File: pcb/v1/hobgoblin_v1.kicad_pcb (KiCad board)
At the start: 2 copper layers, 54 parts, among them J1 5V, J2 RC2014EXT1, J3 RC2014EXT2, J4 USB_B_Mini, SW1 RESET, SW2 ROMBNK, U1 74LS32, U10 FT232RL, U2 Z80CPU, U3 74LS14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

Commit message: Place components on the PCB layout
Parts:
- J2, J3: footprint Connector_PinHeader_2.54mm:PinHeader_1x40_P2.54mm_Vertical -> hobgoblin:RC2014_Connector
- R11: value 330 -> 1K
- moved C12 183.3 mm to (57.0, 106.5), turned to 180 degrees
- moved C11 164.8 mm to (31.0, 68.2), turned to 90 degrees
- moved C9 146.9 mm to (55.0, 68.5), turned to 90 degrees
- moved C1 144.6 mm to (97.5, 110.0), turned to 90 degrees
- moved C3 142.4 mm to (45.7, 68.5), turned to 90 degrees
- moved R6 140.5 mm to (113.5, 30.5), turned to 180 degrees
- moved R2 135.3 mm to (94.5, 89.5), turned to 270 degrees
- moved R8 132.6 mm to (114.0, 89.5), turned to 270 degrees
- moved C6 132.5 mm to (73.5, 107.0), turned to 180 degrees
- moved J2 131.1 mm to (28.0, 25.0), turned to 0 degrees
- moved JP1 118.9 mm to (159.5, 31.0), turned to 180 degrees
- moved J3 116.4 mm to (42.7, 25.0), turned to 0 degrees
- moved D1 113.6 mm to (89.5, 98.5), turned to 90 degrees
- moved C7 107.0 mm to (105.5, 107.0), turned to 180 degrees
- moved C10 106.7 mm to (121.5, 105.0), turned to 180 degrees
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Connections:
- D5 pad 1: Net-(D5-Pad1) -> GND
- D5 pad 2: VCC -> Net-(D5-Pad2)
- R11 pad 2: Net-(D2-Pad2) -> Net-(D5-Pad2)
- U3 pad 14: (no net) -> VCC
- U3 pad 7: (no net) -> GND
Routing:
- added copper zone on B.Cu, net GND
- added copper zone on F.Cu, net GND
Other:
- board outline added: 160 x 110 mm
- board text added: "Pin1"

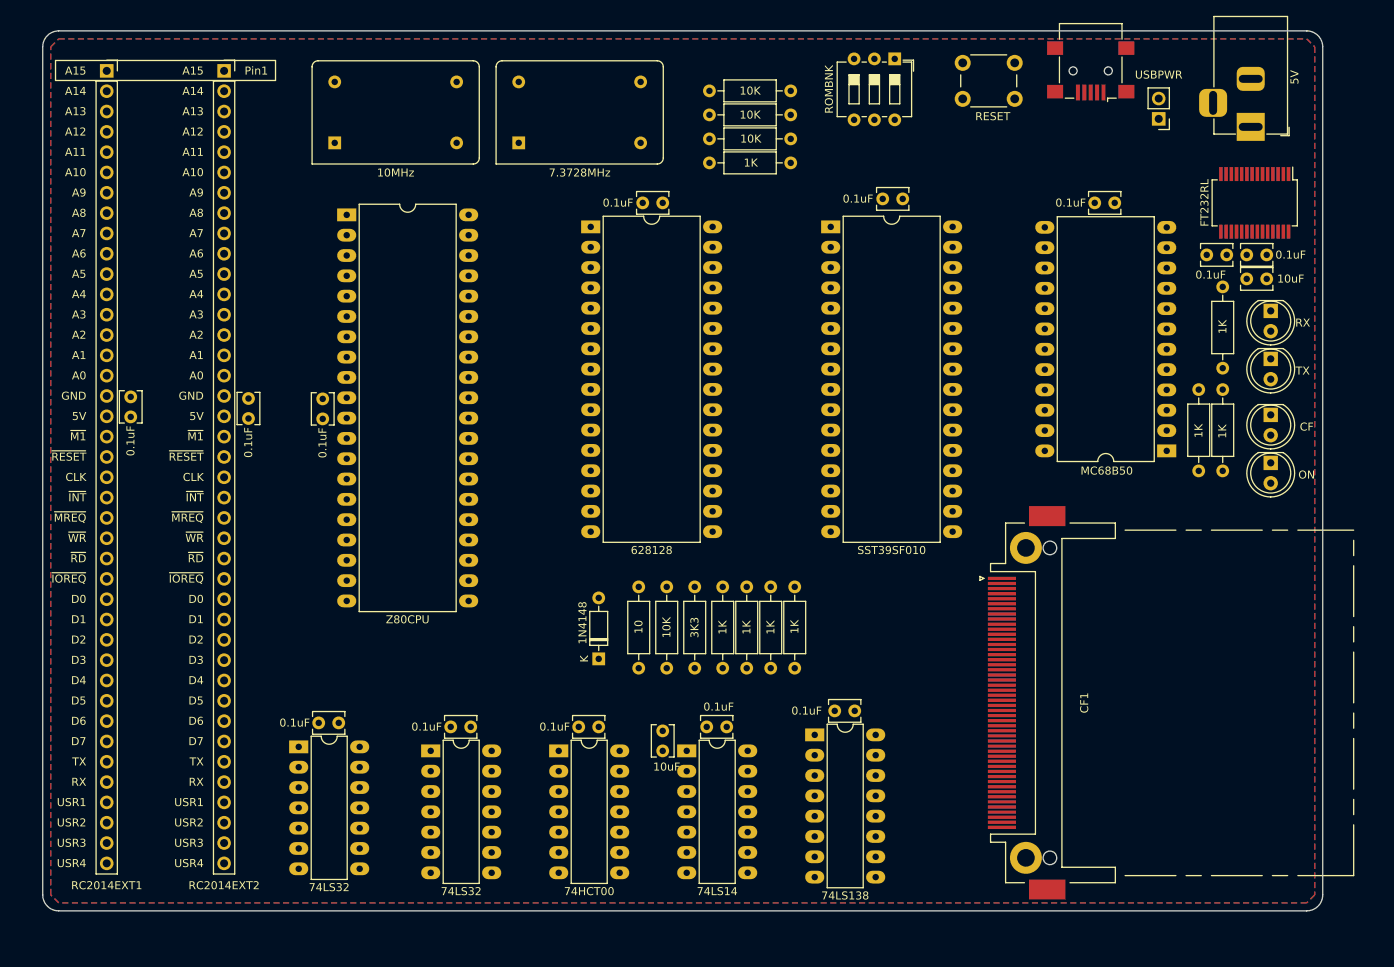
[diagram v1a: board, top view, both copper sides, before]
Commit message: Finish PCB layout
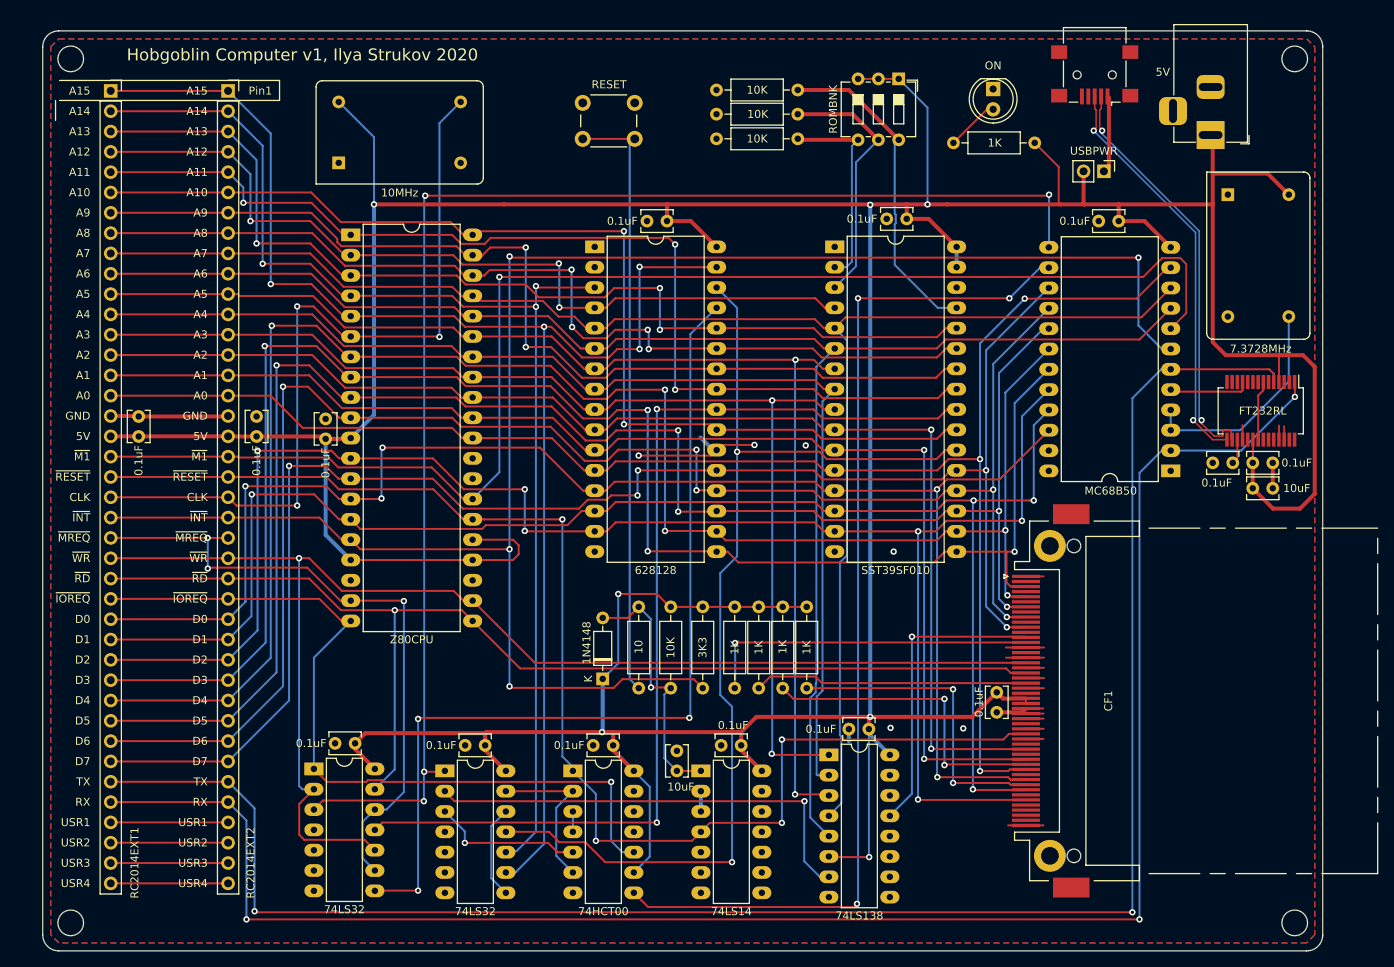
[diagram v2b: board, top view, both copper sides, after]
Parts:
- removed D2: CF, LED_THT:LED_D5.0mm
- removed D3: TX, LED_THT:LED_D5.0mm
- removed D4: RX, LED_THT:LED_D5.0mm
- removed R12, R13, R14: 1K, Resistor_THT:R_Axial_DIN0207_L6.3mm_D2.5mm_P10.16mm_Horizontal
- added C16: 0.1uF, Capacitor_THT:C_Disc_D3.8mm_W2.6mm_P2.50mm, F.Cu at (139.3, 102.7)
- added REF**: M3, MountingHole:MountingHole_3.2mm_M3, F.Cu at (176.5, 131.5)
- added REF**: M3, MountingHole:MountingHole_3.2mm_M3, F.Cu at (23.5, 131.5)
- added REF**: M3, MountingHole:MountingHole_3.2mm_M3, F.Cu at (23.5, 23.5)
- added REF**: M3, MountingHole:MountingHole_3.2mm_M3, F.Cu at (176.5, 23.5)
- moved X2 88.9 mm to (168.1, 40.5), turned to 270 degrees
- moved D5 58.2 mm to (138.8, 27.3)
- moved SW1 47.8 mm to (87.5, 29.0)
- moved R11 45.8 mm to (144.0, 34.0), turned to 180 degrees
- moved C13 26.2 mm to (171.3, 77.2)
- moved C14 26.0 mm to (171.3, 74.0)
- moved C15 26.0 mm to (166.3, 74.0)
- moved U10 26.0 mm to (172.3, 67.5)
- moved JP1 9.48 mm to (152.6, 37.6), turned to 270 degrees
- moved R7 7.91 mm to (115.5, 92.0)
- moved R4 6.05 mm to (114.4, 33.5)
- moved R10 5.15 mm to (106.5, 92.0)
- moved R9 5.15 mm to (109.5, 92.0)
- moved J1 5.11 mm to (166.0, 33.0)
- moved U1 3.34 mm to (53.9, 112.3)
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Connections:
- net Net-(J4-Pad2) renamed /USB_UART/USBD-
- net Net-(J4-Pad3) renamed /USB_UART/USBD+
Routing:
- net VCC: track 0.00 -> 635.4 mm, vias 0 -> 7
- net /TXD: track 0.00 -> 226.7 mm, vias 0 -> 2
- net /RXD: track 0.00 -> 223.0 mm, vias 0 -> 3
- net /~INT: track 0.00 -> 222.8 mm, vias 0 -> 4
- net /D4: track 0.00 -> 213.9 mm, vias 0 -> 5
- net /D2: track 0.00 -> 211.5 mm, vias 0 -> 6
- net /D5: track 0.00 -> 208.0 mm, vias 0 -> 5
- net /D3: track 0.00 -> 206.2 mm, vias 0 -> 4
- net /D6: track 0.00 -> 205.7 mm, vias 0 -> 5
- net /A6: track 0.00 -> 202.6 mm
- net /A7: track 0.00 -> 202.1 mm
- net /A0: track 0.00 -> 201.1 mm, vias 0 -> 3
- net /D7: track 0.00 -> 198.0 mm, vias 0 -> 5
- net /D0: track 0.00 -> 193.8 mm, vias 0 -> 5
- net /D1: track 0.00 -> 190.9 mm, vias 0 -> 4
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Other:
- board size 160 x 110 mm -> 160 x 115 mm
- board text added: "Hobgoblin Computer v1, Ilya Strukov 2020"

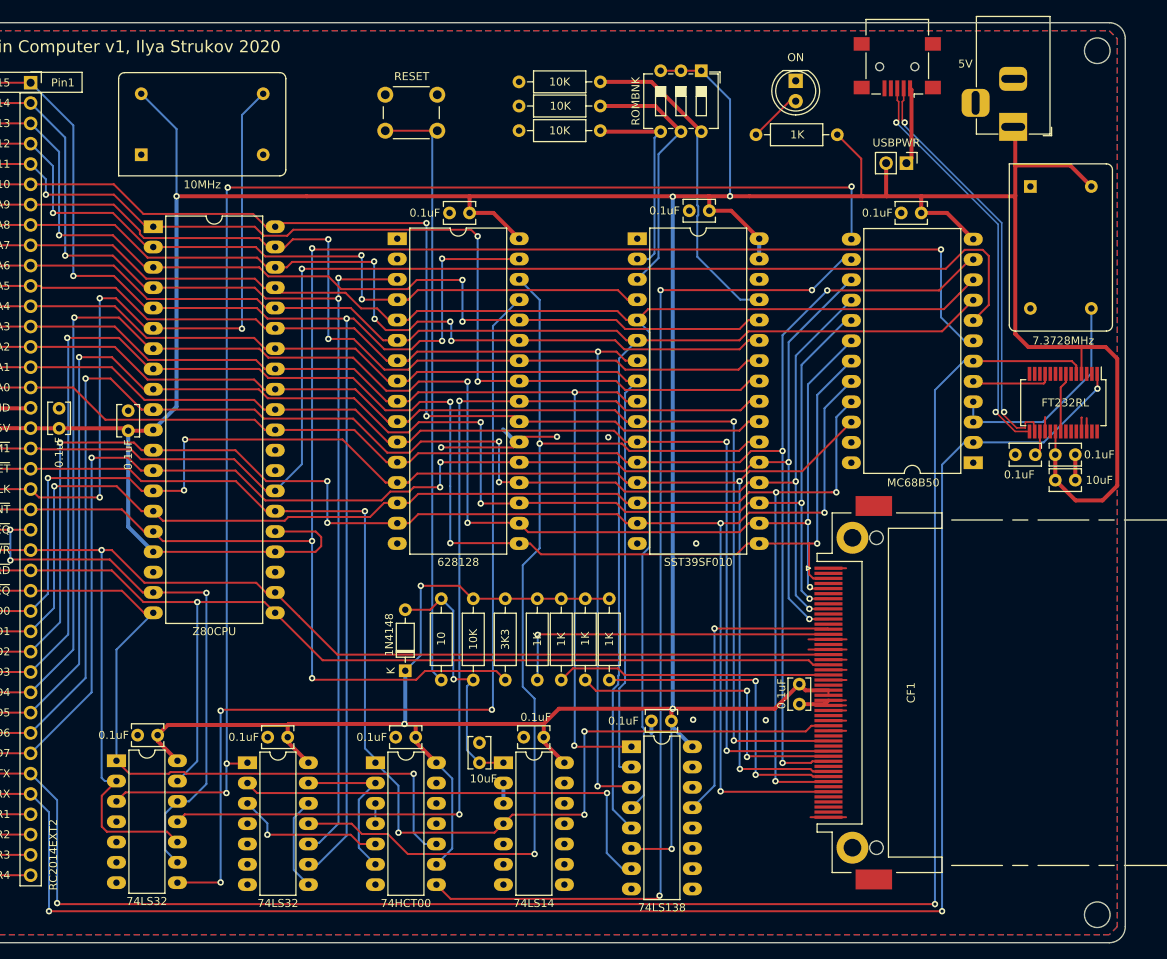
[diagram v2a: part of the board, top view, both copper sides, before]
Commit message: Add UART socket and other PCB improvements
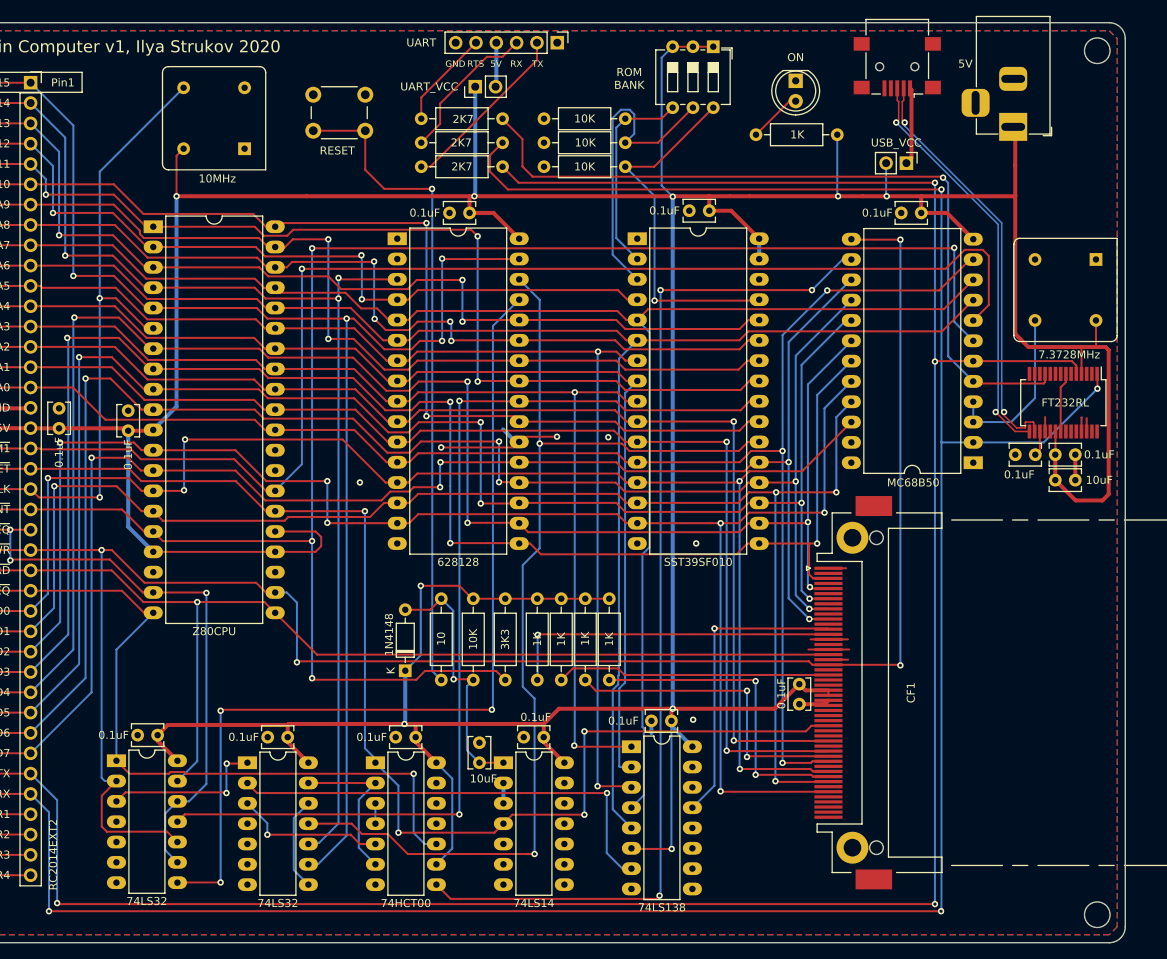
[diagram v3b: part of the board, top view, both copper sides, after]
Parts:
- added J5: UART, Connector_PinHeader_2.54mm:PinHeader_1x06_P2.54mm_Vertical, F.Cu at (109.0, 22.5)
- added JP2: UART_VCC, Connector_PinHeader_2.54mm:PinHeader_1x02_P2.54mm_Vertical, F.Cu at (98.8, 28.0)
- added R12: 2K7, Resistor_THT:R_Axial_DIN0207_L6.3mm_D2.5mm_P10.16mm_Horizontal, F.Cu at (92.0, 38.0)
- added R13: 2K7, Resistor_THT:R_Axial_DIN0207_L6.3mm_D2.5mm_P10.16mm_Horizontal, F.Cu at (92.0, 35.0)
- added R14: 2K7, Resistor_THT:R_Axial_DIN0207_L6.3mm_D2.5mm_P10.16mm_Horizontal, F.Cu at (92.0, 32.0)
- JP1: value USBPWR -> USB_VCC
- X1, X2: footprint Oscillator:Oscillator_DIP-14 -> Oscillator:Oscillator_DIP-8
- moved X1 12.9 mm to (69.9, 35.8), turned to 90 degrees
- moved X2 12.3 mm to (176.3, 49.6), turned to 180 degrees
- moved R6 11.1 mm to (117.5, 38.0)
- moved SW1 9.00 mm to (78.5, 29.0)
- moved R5 5.55 mm to (117.5, 35.0)
- moved R4 3.46 mm to (117.5, 32.0)
- moved SW2 3.35 mm to (128.5, 23.0)
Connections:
- CF1 pad 34: /~WR -> /~RD
- CF1 pad 35: /~RD -> /~WR
- U9 pad 13: /~IOWR -> /~WR
- X1 pad 8: /CPU_CLK -> VCC
- X2 pad 8: /UART_CLK -> VCC
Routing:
- net /~IOWR: track 177.3 -> 20.6 mm, vias 4 -> 2
- net /RXD: track 223.0 -> 317.8 mm, vias 3 -> 4
- net /~RTS: track 10.2 -> 97.4 mm, vias 0 -> 1
- net /TXD: track 226.7 -> 306.1 mm, vias 2 -> 4
- net /~WR: track 167.0 -> 240.4 mm, vias 1 -> 4
- net Net-(J5-Pad2): track 0.00 -> 22.2 mm
- net GND: track 88.3 -> 69.0 mm
- net Net-(J5-Pad3): track 0.00 -> 18.6 mm
- net Net-(J5-Pad5): track 0.00 -> 12.3 mm
- net /CPU_CLK: track 98.5 -> 87.5 mm, vias 3 -> 2
- net /ROMBNK1: track 32.1 -> 39.1 mm
- net /UART_CLK: track 27.9 -> 21.2 mm
- net Net-(R2-Pad2): track 75.9 -> 82.6 mm, vias 0 -> 1
- net Net-(J5-Pad4): track 0.00 -> 5.54 mm
- net /ROMBNK0: track 41.1 -> 45.4 mm, vias 0 -> 1
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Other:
- board text added: "5V"
- board text added: "GND"
- board text added: "ROM BANK"
- board text added: "RTS"
- board text added: "RX"
- board text added: "TX"

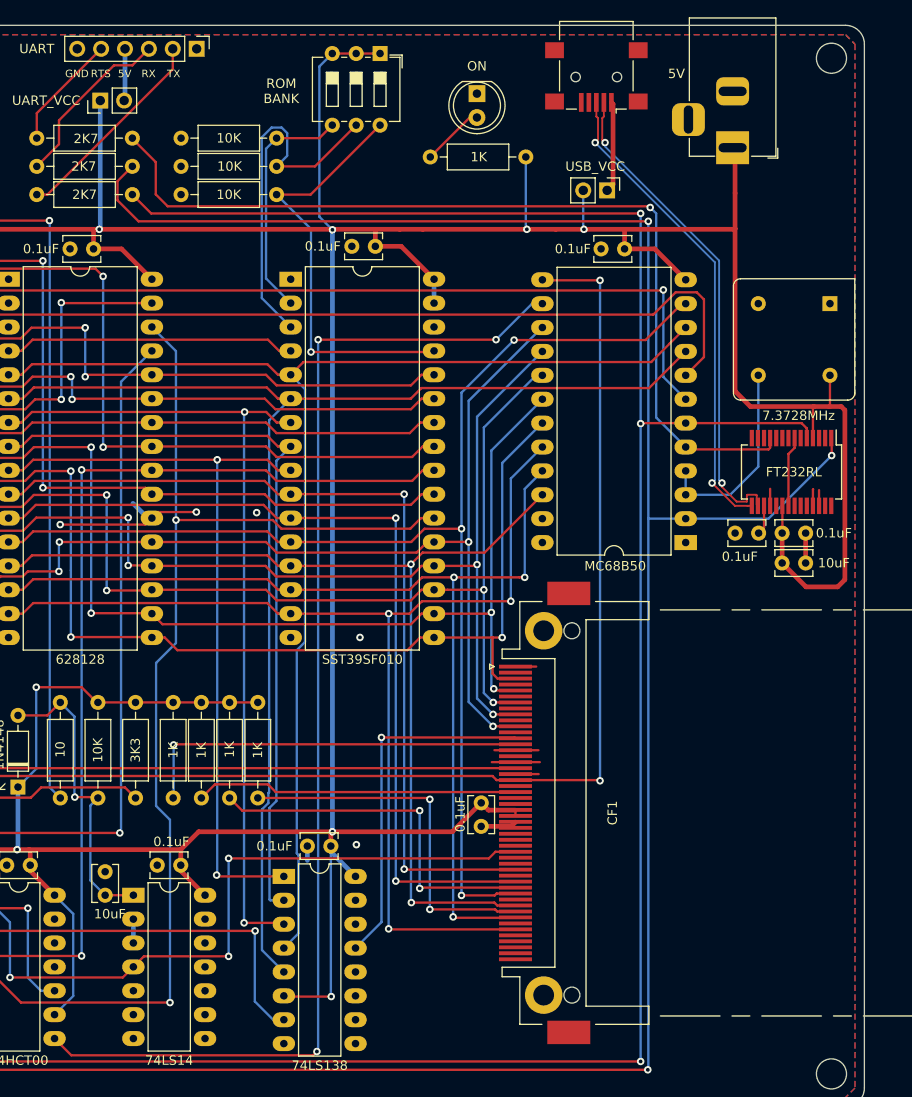
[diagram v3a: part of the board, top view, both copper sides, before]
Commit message: Add CF busy LED
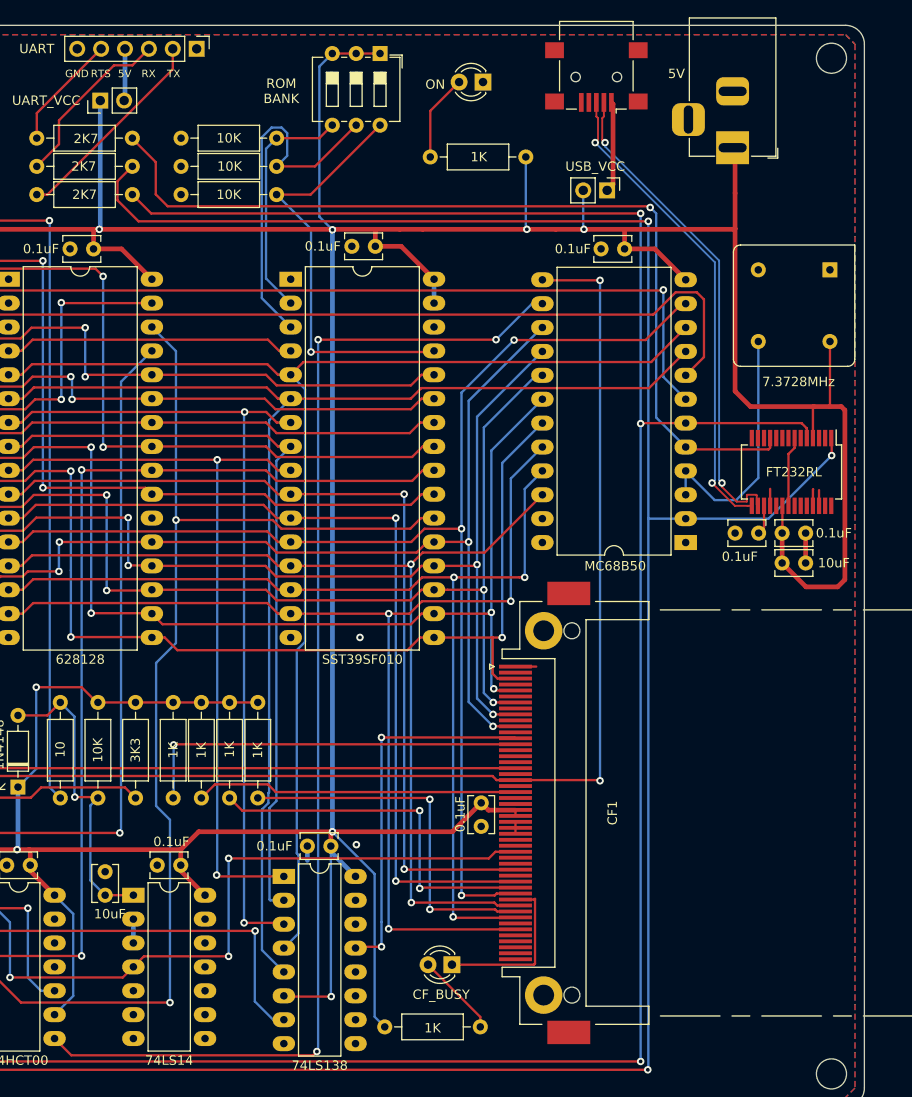
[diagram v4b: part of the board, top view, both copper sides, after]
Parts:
- added D2: CF_BUSY, LED_THT:LED_D3.0mm, F.Cu at (136.1, 119.9)
- added R15: 1K, Resistor_THT:R_Axial_DIN0207_L6.3mm_D2.5mm_P10.16mm_Horizontal, F.Cu at (129.0, 126.5)
- D5: footprint LED_THT:LED_D5.0mm -> LED_THT:LED_D3.0mm
- moved X2 3.59 mm to (176.3, 46.0)
- moved D5 1.39 mm to (139.4, 26.0), turned to 180 degrees
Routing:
- net GND: track 69.0 -> 36.5 mm, vias 6 -> 3
- net VCC: track 634.0 -> 660.7 mm
- net Net-(CF1-Pad45): track 0.00 -> 17.9 mm
- net Net-(D2-Pad2): track 0.00 -> 8.91 mm
- net /UART_CLK: track 21.2 -> 27.0 mm
- net Net-(D5-Pad2): track 6.70 -> 9.23 mm
- net /~PORT10: track 37.8 -> 39.4 mm, vias 1 -> 2
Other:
- board text added: "160x115mm"
